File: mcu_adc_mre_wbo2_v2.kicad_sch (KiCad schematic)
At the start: 54 parts, among them J1 TC2030, J2 Conn_01x06_Male, J3 Conn_01x03_Male, SW1 SW_Push, U1 STM32F072CBUx, U2 MCP6004, U3 AD8628, U4 REF3033, Y1 8MHz

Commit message: V2.5 with OPAmp
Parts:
- removed SW1: SW_Push, rusefi_lib:SW_SPST_CK_RS282G05A3, symbol Switch:SW_Push
- added BOOT_TP1: TestPoint_2Pole, TestPoint:TestPoint_Bridge_Pitch2.54mm_Drill0.7mm, symbol Connector:TestPoint_2Pole
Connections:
- net +3V3: now also BOOT_TP1.1
- net Boot0: now also BOOT_TP1.2
- net DAC2: now reaches U1.14 (PA4)
- net DAC1: now reaches U1.15 (PA5)
- no-connect marks 20 -> 18

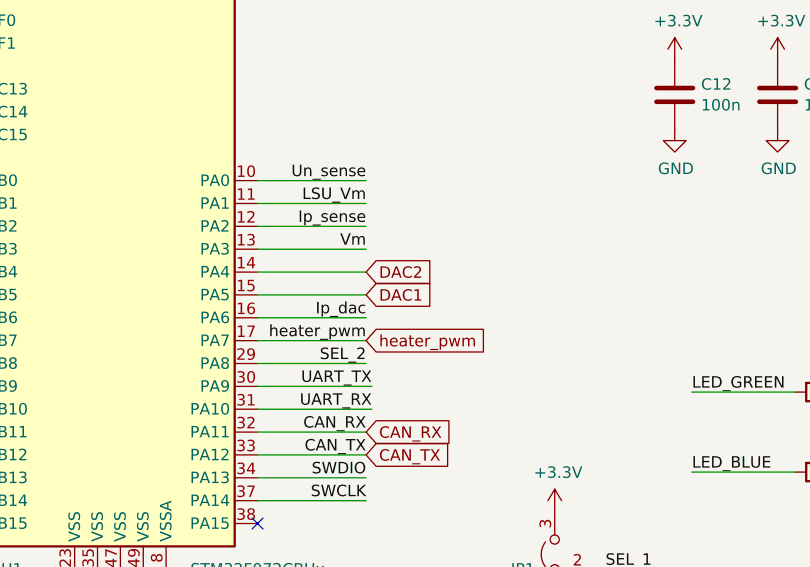
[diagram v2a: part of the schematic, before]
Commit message: some changes on DAC pins
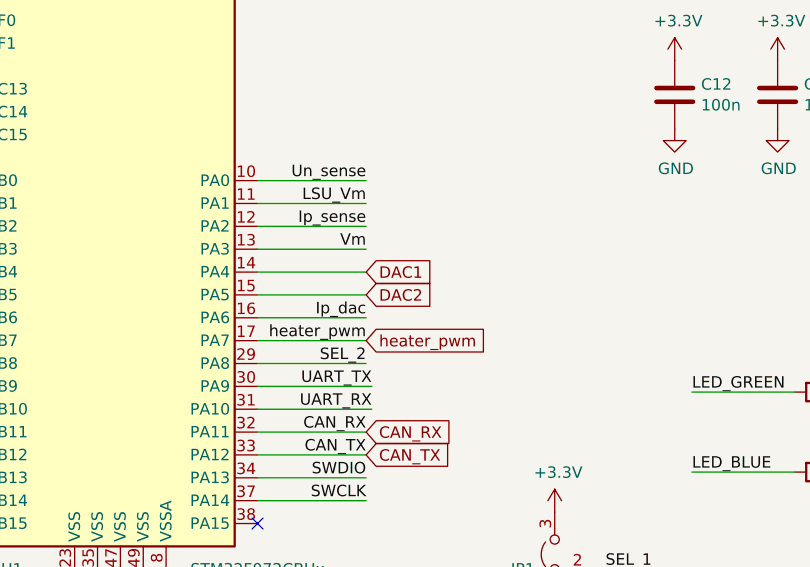
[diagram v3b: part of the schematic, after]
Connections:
- net DAC1: now also U1.14 (PA4); no longer U1.15 (PA5)
- net DAC2: now also U1.15 (PA5); no longer U1.14 (PA4)
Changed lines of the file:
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@@
   (title_block
     (title "MRE addon board V2- WBO2 & EGT & SD Card")
-    (date "2023-01-31")
+    (date "2023-02-05")
     (rev "V2.5")
     (company "by JRD McLAREN")
@@
     (stroke (width 0) (type default) (color 0 0 0 0))
   )
+  (wire (pts (xy 196.85 97.79) (xy 208.915 97.79))
+    (stroke (width 0) (type default) (color 0 0 0 0))
+  )
   (wire (pts (xy 196.85 90.17) (xy 208.915 90.17))
     (stroke (width 0) (type default) (color 0 0 0 0))
@@
     (stroke (width 0) (type default) (color 0 0 0 0))
   )
+  (wire (pts (xy 196.85 95.25) (xy 208.915 95.25))
+    (stroke (width 0) (type default) (color 0 0 0 0))
+  )
   (wire (pts (xy 27.94 29.845) (xy 27.94 32.385))
     (stroke (width 0) (type default) (color 0 0 0 0))
@@
     (stroke (width 0) (type default) (color 0 0 0 0))
   )
-  (wire (pts (xy 196.85 95.25) (xy 208.915 95.25))
-    (stroke (width 0) (type default) (color 0 0 0 0))
-  )
   (wire (pts (xy 95.885 89.535) (xy 97.155 89.535))
     (stroke (width 0) (type default) (color 0 0 0 0))
@@
   )
   (wire (pts (xy 158.75 66.04) (xy 163.83 66.04))
-    (stroke (width 0) (type default) (color 0 0 0 0))
-  )
-  (wire (pts (xy 196.85 97.79) (xy 208.915 97.79))
     (stroke (width 0) (type default) (color 0 0 0 0))
   )
@@
     )
   )
-  (global_label "DAC2" (shape input) (at 208.915 95.25 0) (fields_autoplaced)
+  (global_label "DAC2" (shape input) (at 208.915 97.79 0) (fields_autoplaced)
+    (effects (font (size 1.27 1.27)) (justify left))
+    (property "Medzirezortné odkazy" "${INTERSHEET_REFS}" (id 0) (at 216.0773 97.7106 0)
+      (effects (font (size 1.27 1.27)) (justify left) hide)
+    )
+  )
+  (global_label "DAC1" (shape input) (at 208.915 95.25 0) (fields_autoplaced)
     (effects (font (size 1.27 1.27)) (justify left))
     (property "Medzirezortné odkazy" "${INTERSHEET_REFS}" (id 0) (at 216.0773 95.1706 0)
       (effects (font (size 1.27 1.27)) (justify left) hide)
     )
-  )
-  (global_label "DAC1" (shape input) (at 208.915 97.79 0) (fields_autoplaced)
-    (effects (font (size 1.27 1.27)) (justify left))
-    (property "Medzirezortné odkazy" "${INTERSHEET_REFS}" (id 0) (at 216.0773 97.7106 0)
-      (effects (font (size 1.27 1.27)) (justify left) hide)
-    )

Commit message: V2.5 - 13.02.2023
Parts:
- added PA15, PB0, PB10, PB11, PB12, PB13, PB14, PB15, PB3, PB4, PB8, PB9: TestPoint, TestPoint:TestPoint_Pad_D1.0mm, symbol Connector:TestPoint
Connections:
- net at U1.18 (PB0): now also PB0.1
- net at U1.21 (PB10): now also PB10.1
- net at U1.22 (PB11): now also PB11.1
- net at U1.25 (PB12): now also PB12.1
- net at U1.26 (PB13): now also PB13.1
- net at U1.27 (PB14): now also PB14.1
- net at U1.28 (PB15): now also PB15.1
- net at U1.38 (PA15): now also PA15.1
- net at U1.39 (PB3): now also PB3.1
- net at U1.40 (PB4): now also PB4.1
- net at U1.45 (PB8): now also PB8.1
- net at U1.46 (PB9): now also PB9.1
- no-connect marks 18 -> 6
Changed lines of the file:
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@@
   (title_block
     (title "MRE addon board V2- WBO2 & EGT & SD Card")
-    (date "2023-02-05")
+    (date "2023-02-13")
     (rev "V2.5")
     (company "by JRD McLAREN")
@@
   (junction (at 114.935 86.995) (diameter 0) (color 0 0 0 0)
   )
-  (no_connect (at 163.83 92.71))
-  (no_connect (at 163.83 105.41))
-  (no_connect (at 196.85 123.19))
   (no_connect (at 163.83 74.93))
-  (no_connect (at 163.83 95.25))
-  (no_connect (at 163.83 107.95))
-  (no_connect (at 163.83 110.49))
-  (no_connect (at 163.83 120.65))
   (no_connect (at 130.81 183.515))
-  (no_connect (at 163.83 115.57))
-  (no_connect (at 163.83 123.19))
   (no_connect (at 163.83 77.47))
-  (no_connect (at 163.83 118.11))
   (no_connect (at 91.44 182.88))
   (no_connect (at 163.83 90.17))
   (no_connect (at 163.83 80.01))
-  (no_connect (at 163.83 113.03))
-  (no_connect (at 163.83 85.09))
   (wire (pts (xy 245.11 117.475) (xy 256.54 117.475))
     (stroke (width 0) (type default) (color 0 0 0 0))
@@
     (pin "1")
   )
+  (symbol (lib_id "Connector:TestPoint") (at 163.83 110.49 90) (unit 1)
+    (in_bom no) (on_board yes)
+    (property "Reference" "PB10" (id 0) (at 155.575 110.49 90))
+    (property "Value" "TestPoint" (id 1) (at 160.528 108.6921 90)
+      (effects (font (size 1.27 1.27)) hide)
+    )
+    (property "Footprint" "TestPoint:TestPoint_Pad_D1.0mm" (id 2) (at 163.83 105.41 0)
+      (effects (font (size 1.27 1.27)) hide)
+    )
+    (property "Datasheet" "~" (id 3) (at 163.83 105.41 0)
+      (effects (font (size 1.27 1.27)) hide)
+    )
+    (pin "1")
+  )
   (symbol (lib_id "Device:C") (at 153.035 71.12 90) (unit 1)
     (in_bom yes) (on_board yes)
@@
     (pin "2")
   )
+  (symbol (lib_id "Connector:TestPoint") (at 163.83 105.41 90) (unit 1)
+    (in_bom no) (on_board yes)
+    (property "Reference" "PB8" (id 0) (at 154.94 105.41 90))
+    (property "Value" "TestPoint" (id 1) (at 160.528 103.6121 90)
+      (effects (font (size 1.27 1.27)) hide)
+    )
+    (property "Footprint" "TestPoint:TestPoint_Pad_D1.0mm" (id 2) (at 163.83 100.33 0)
+      (effects (font (size 1.27 1.27)) hide)
+    )
+    (property "Datasheet" "~" (id 3) (at 163.83 100.33 0)
+      (effects (font (size 1.27 1.27)) hide)
+    )
+    (pin "1")
+  )
+  (symbol (lib_id "Connector:TestPoint") (at 163.83 85.09 90) (unit 1)
+    (in_bom no) (on_board yes)
+    (property "Reference" "PB0" (id 0) (at 156.845 85.09 90))
+    (property "Value" "TestPoint" (id 1) (at 160.528 83.2921 90)
+      (effects (font (size 1.27 1.27)) hide)
+    )
+    (property "Footprint" "TestPoint:TestPoint_Pad_D1.0mm" (id 2) (at 163.83 80.01 0)
+      (effects (font (size 1.27 1.27)) hide)
+    )
+    (property "Datasheet" "~" (id 3) (at 163.83 80.01 0)
+      (effects (font (size 1.27 1.27)) hide)
+    )
+    (pin "1")
+  )
+  (symbol (lib_id "Connector:TestPoint") (at 163.83 120.65 90) (unit 1)
+    (in_bom no) (on_board yes)
+    (property "Reference" "PB14" (id 0) (at 155.575 120.65 90))
+    (property "Value" "TestPoint" (id 1) (at 160.528 118.8521 90)
+      (effects (font (size 1.27 1.27)) hide)
+    )
+    (property "Footprint" "TestPoint:TestPoint_Pad_D1.0mm" (id 2) (at 163.83 115.57 0)
+      (effects (font (size 1.27 1.27)) hide)
+    )
+    (property "Datasheet" "~" (id 3) (at 163.83 115.57 0)
+      (effects (font (size 1.27 1.27)) hide)
+    )
+    (pin "1")
+  )
   (symbol (lib_id "Connector:TestPoint_2Pole") (at 264.795 76.835 270) (unit 1)
     (in_bom yes) (on_board yes) (fields_autoplaced)
@@
     (pin "2")
   )
+  (symbol (lib_id "Connector:TestPoint") (at 163.83 92.71 90) (unit 1)
+    (in_bom no) (on_board yes)
+    (property "Reference" "PB3" (id 0) (at 156.845 92.71 90))
+    (property "Value" "TestPoint" (id 1) (at 160.528 90.9121 90)
+      (effects (font (size 1.27 1.27)) hide)
+    )
+    (property "Footprint" "TestPoint:TestPoint_Pad_D1.0mm" (id 2) (at 163.83 87.63 0)
+      (effects (font (size 1.27 1.27)) hide)
+    )
+    (property "Datasheet" "~" (id 3) (at 163.83 87.63 0)
+      (effects (font (size 1.27 1.27)) hide)
+    )
+    (pin "1")
+  )
+  (symbol (lib_id "Connector:TestPoint") (at 163.83 118.11 90) (unit 1)
+    (in_bom no) (on_board yes)
+    (property "Reference" "PB13" (id 0) (at 155.575 118.11 90))
+    (property "Value" "TestPoint" (id 1) (at 160.528 116.3121 90)
+      (effects (font (size 1.27 1.27)) hide)
+    )
+    (property "Footprint" "TestPoint:TestPoint_Pad_D1.0mm" (id 2) (at 163.83 113.03 0)
+      (effects (font (size 1.27 1.27)) hide)
+    )
+    (property "Datasheet" "~" (id 3) (at 163.83 113.03 0)
+      (effects (font (size 1.27 1.27)) hide)
+    )
+    (pin "1")
+  )
+  (symbol (lib_id "Connector:TestPoint") (at 163.83 115.57 90) (unit 1)
+    (in_bom no) (on_board yes)
+    (property "Reference" "PB12" (id 0) (at 155.575 115.57 90))
+    (property "Value" "TestPoint" (id 1) (at 160.528 113.7721 90)
+      (effects (font (size 1.27 1.27)) hide)
+    )
+    (property "Footprint" "TestPoint:TestPoint_Pad_D1.0mm" (id 2) (at 163.83 110.49 0)
+      (effects (font (size 1.27 1.27)) hide)
+    )
+    (property "Datasheet" "~" (id 3) (at 163.83 110.49 0)
+      (effects (font (size 1.27 1.27)) hide)
+    )
+    (pin "1")
+  )
+  (symbol (lib_id "Connector:TestPoint") (at 196.85 123.19 270) (unit 1)
+    (in_bom no) (on_board yes)
+    (property "Reference" "PA15" (id 0) (at 202.565 123.19 90)
+      (effects (font (size 1.27 1.27)) (justify left))
+    )
+    (property "Value" "TestPoint" (id 1) (at 201.549 124.8922 90)
+      (effects (font (size 1.27 1.27)) (justify left) hide)
+    )
+    (property "Footprint" "TestPoint:TestPoint_Pad_D1.0mm" (id 2) (at 196.85 128.27 0)
+      (effects (font (size 1.27 1.27)) hide)
+    )
+    (property "Datasheet" "~" (id 3) (at 196.85 128.27 0)
+      (effects (font (size 1.27 1.27)) hide)
+    )
+    (pin "1")
+  )
   (symbol (lib_id "power:GND") (at 140.335 68.58 270) (unit 1)
     (in_bom yes) (on_board yes) (fields_autoplaced)
@@
     (pin "1")
   )
+  (symbol (lib_id "Connector:TestPoint") (at 163.83 123.19 90) (unit 1)
+    (in_bom no) (on_board yes)
+    (property "Reference" "PB15" (id 0) (at 155.575 123.19 90))
+    (property "Value" "TestPoint" (id 1) (at 160.528 121.3921 90)
+      (effects (font (size 1.27 1.27)) hide)
+    )
+    (property "Footprint" "TestPoint:TestPoint_Pad_D1.0mm" (id 2) (at 163.83 118.11 0)
+      (effects (font (size 1.27 1.27)) hide)
+    )
+    (property "Datasheet" "~" (id 3) (at 163.83 118.11 0)
+      (effects (font (size 1.27 1.27)) hide)
+    )
+    (pin "1")
+  )
+  (symbol (lib_id "Connector:TestPoint") (at 163.83 107.95 90) (unit 1)
+    (in_bom no) (on_board yes)
+    (property "Reference" "PB9" (id 0) (at 154.94 107.95 90))
+    (property "Value" "TestPoint" (id 1) (at 160.528 106.1521 90)
+      (effects (font (size 1.27 1.27)) hide)
+    )
+    (property "Footprint" "TestPoint:TestPoint_Pad_D1.0mm" (id 2) (at 163.83 102.87 0)
+      (effects (font (size 1.27 1.27)) hide)
+    )
+    (property "Datasheet" "~" (id 3) (at 163.83 102.87 0)
+      (effects (font (size 1.27 1.27)) hide)
+    )
+    (pin "1")
+  )
+  (symbol (lib_id "Connector:TestPoint") (at 163.83 95.25 90) (unit 1)
+    (in_bom no) (on_board yes)
+    (property "Reference" "PB4" (id 0) (at 156.845 95.25 90))
+    (property "Value" "TestPoint" (id 1) (at 160.528 93.4521 90)
+      (effects (font (size 1.27 1.27)) hide)
+    )
+    (property "Footprint" "TestPoint:TestPoint_Pad_D1.0mm" (id 2) (at 163.83 90.17 0)
+      (effects (font (size 1.27 1.27)) hide)
+    )
+    (property "Datasheet" "~" (id 3) (at 163.83 90.17 0)
+      (effects (font (size 1.27 1.27)) hide)
+    )
+    (pin "1")
+  )
   (symbol (lib_id "Device:C") (at 153.035 66.04 90) (unit 1)
     (in_bom yes) (on_board yes)
@@
     (pin "2")
   )
+  (symbol (lib_id "Connector:TestPoint") (at 163.83 113.03 90) (unit 1)
+    (in_bom no) (on_board yes)
+    (property "Reference" "PB11" (id 0) (at 155.575 113.03 90))
+    (property "Value" "TestPoint" (id 1) (at 160.528 111.2321 90)
+      (effects (font (size 1.27 1.27)) hide)
+    )
+    (property "Footprint" "TestPoint:TestPoint_Pad_D1.0mm" (id 2) (at 163.83 107.95 0)
+      (effects (font (size 1.27 1.27)) hide)
+    )
+    (property "Datasheet" "~" (id 3) (at 163.83 107.95 0)
+      (effects (font (size 1.27 1.27)) hide)
+    )
+    (pin "1")
+  )
   (sheet_instances
